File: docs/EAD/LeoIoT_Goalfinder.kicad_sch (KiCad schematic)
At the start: 38 parts, among them J1 USB_B_Micro_Breakout, J1e1 Conn_01x02_Pin, J2 LED Strip, J3 GAIN, Q1 IRFZ44N, U1 ESP32_D1_mini, U2 VL53L0X_Breakout, U3 MAX98357A_Breakout, U4 SW420_Breakout, U5 LIS3DH_Breakout

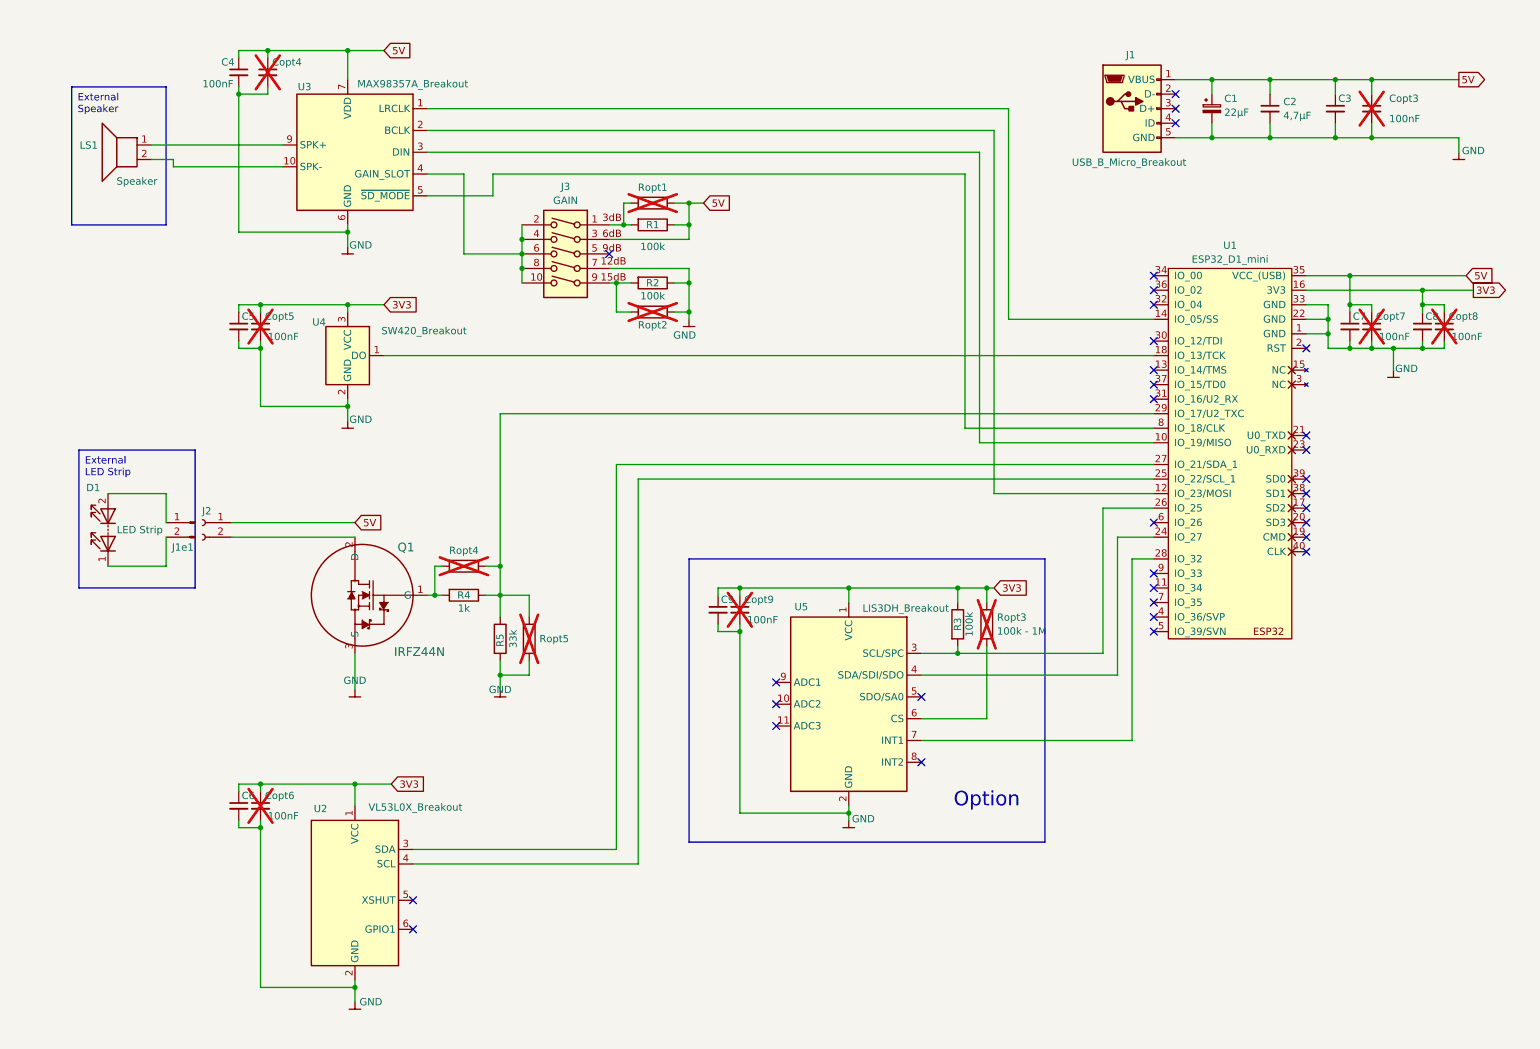
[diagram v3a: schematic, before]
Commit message: added r1.4 of PCB and SMD-only PCB layout as well as production files
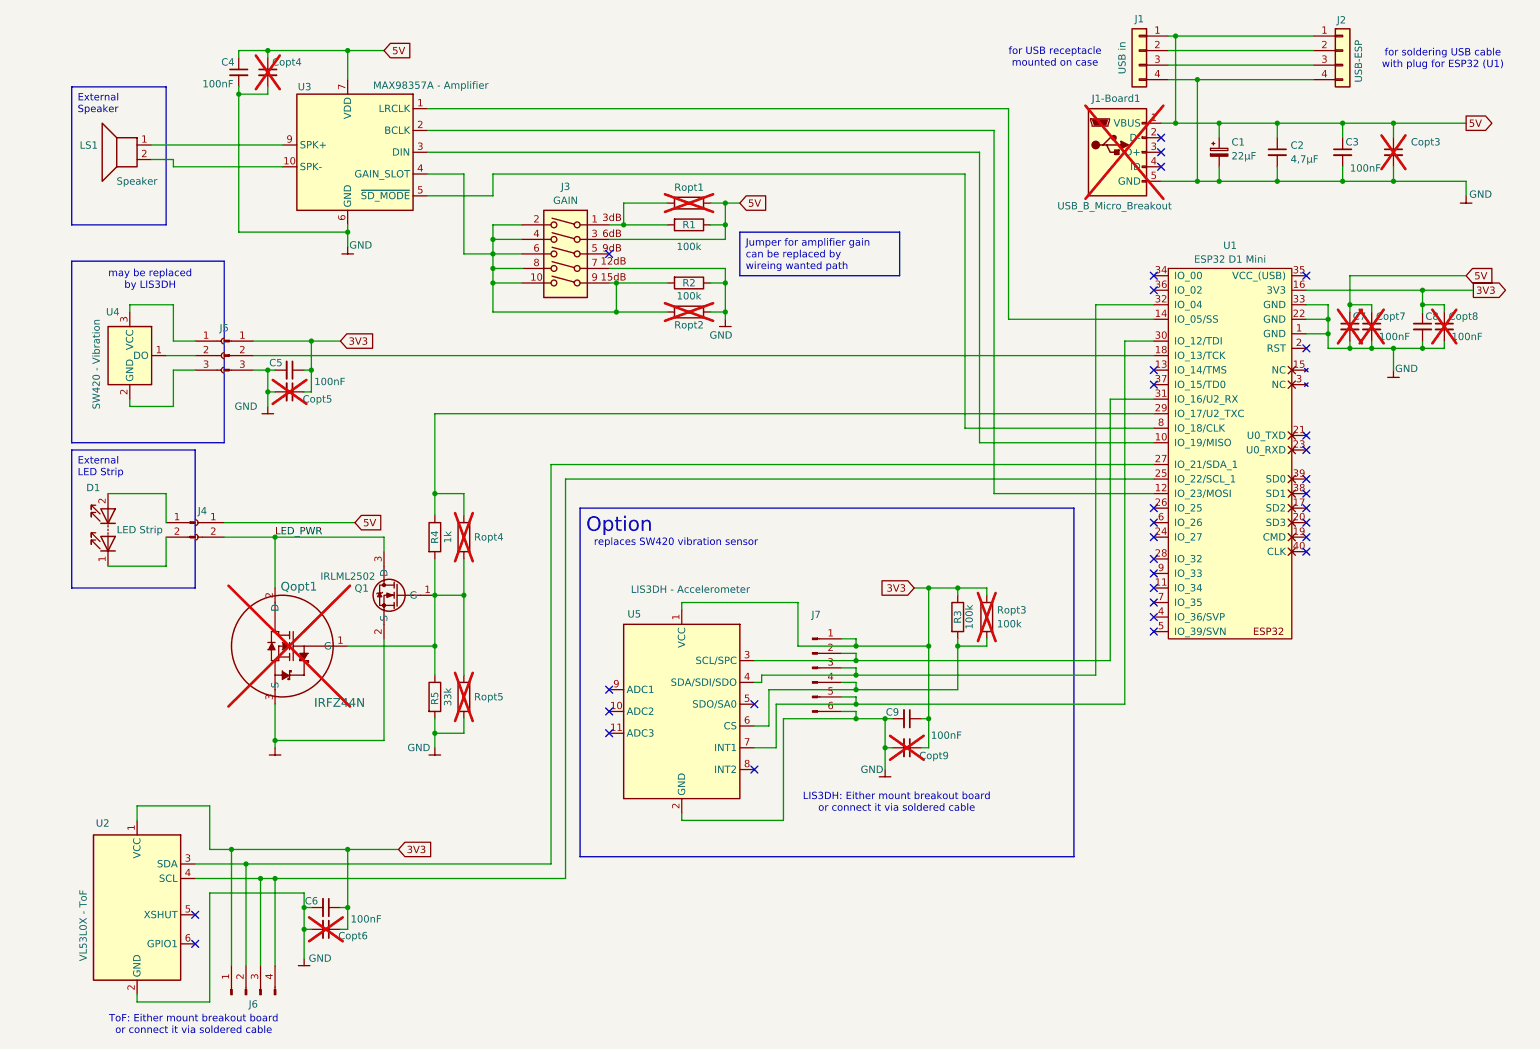
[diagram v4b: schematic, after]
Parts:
- added J1: USB in, Connector_PinHeader_2.54mm:PinHeader_1x04_P2.54mm_Vertical, symbol Connector_Generic:Conn_01x04
- added J2: USB-ESP, Connector_PinHeader_2.54mm:PinHeader_1x04_P2.54mm_Vertical, symbol Connector_Generic:Conn_01x04
- added J5: SW240 - Vcc/D0/GND, Connector_PinHeader_2.54mm:PinHeader_1x03_P2.54mm_Horizontal, symbol Connector:Conn_01x03_Pin
- added J5e1: Conn_01x03_Socket, symbol Connector:Conn_01x03_Socket
- added J6: VL53L0X-ToF Vcc/SDA/SCL/GND, Connector_PinHeader_2.54mm:PinHeader_1x04_P2.54mm_Vertical, symbol Connector:Conn_01x04_Pin
- added J7: LIS3DH, Connector_PinHeader_2.54mm:PinHeader_1x06_P2.54mm_Horizontal, symbol Connector:Conn_01x06_Pin
- added Q1: IRLML2502, Package_TO_SOT_SMD:SOT-23, symbol Transistor_FET_Own:IRLML2502
- C7: now not fitted; now left out of the parts list
- J1-Board1: renamed from J1; now not fitted
- J4: renamed from J2; footprint Connector_JST_2.54:JST_XH_B2B-XH-A_1x02_P2.54mm_Vertical -> Connector_JST:JST_XH_B2B-XH-A_1x02_P2.50mm_Vertical; now left out of the parts list
- Qopt1: renamed from Q1; now not fitted
- R3: now in the parts list
- Ropt3: value 100k - 1M -> 100k
- U1: value ESP32_D1_mini -> ESP32 D1 Mini
- U2: value VL53L0X_Breakout -> VL53L0X - ToF
- U3: value MAX98357A_Breakout -> MAX98357A - Amplifier
- U4: value SW420_Breakout -> SW420 - Vibration
- U5: value LIS3DH_Breakout -> LIS3DH - Accelerometer; now in the parts list
- renumbered J1e1 to J4e1
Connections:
- net 3V3: now also J5.1 (Pin_1), J6.1 (Pin_1), J7.1 (Pin_1); no longer U4.3 (VCC)
- net 5V: now also J1.1 (Pin_1), J2.1 (Pin_1); no longer U1.35 (VCC_(USB))
- net GND: now also J1.4 (Pin_4), J2.4 (Pin_4), J5.3 (Pin_3), J7.6 (Pin_6), Q1.2 (S); no longer U4.2 (GND)
- net at R4.1, Ropt4.1, U1.29 (IO_17/U2_TXC): no longer R5.1, Ropt5.1
- net at J3.10, J3.2, J3.4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: now also J3.9, R2.2, Ropt2.2
- net at Qopt1.1 (G), R4.2, Ropt4.2: now also R5.1, Ropt5.1, Q1.1 (G)
- net at Ropt3.2, U5.6 (CS): now also R3.2, J7.4 (Pin_4)
- net LED_PWR: now reaches J4.2 (Pin_2), Qopt1.2 (D)
- net LED_PWR: now also Q1.3 (D)
- net at U5.4 (SDA/SDI/SDO): now also U1.32 (IO_04), J7.3 (Pin_3); no longer U1.24 (IO_27)
- net at U5.7 (INT1): now also U1.30 (IO_12/TDI), J7.5 (Pin_5); no longer U1.28 (IO_32)
- net at U4.1 (DO): now also J5e1.2 (Pin_2); no longer U1.18 (IO_13/TCK)
- net at U1.27 (IO_21/SDA_1), U2.3 (SDA): now also J6.2 (Pin_2)
- net at U1.25 (IO_22/SCL_1), U2.4 (SCL): now also J6.3 (Pin_3), J6.4 (Pin_4)
- net at U1.31 (IO_16/U2_RX): now also U5.3 (SCL/SPC), J7.2 (Pin_2)
- new net: J1.2 (Pin_2), J2.2 (Pin_2)
- new net: J1.3 (Pin_3), J2.3 (Pin_3)
- new net: J5e1.3 (Pin_3), U4.2 (GND)
- new net: J5e1.1 (Pin_1), U4.3 (VCC)
- new net: J5.2 (Pin_2), U1.18 (IO_13/TCK)
- now unconnected: U1.26 (IO_25)
- no-connect marks 33 -> 34
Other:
- note added: "LIS3DH: Either mount breakout board or connect it via soldered cable"
- note added: "ToF: Either mount breakout board or connect it via soldered cable"
- note added: "for USB receptacle mounted on case"
- note added: "for soldering USB cable with plug for ESP32 (U1)"
- note added: "may be replaced by LIS3DH"
- note added: "replaces SW420 vibration sensor"
- company: HTL Leonding, SJ 23-24, 2BHIF -> HTL Leonding, Leo Cub IoT
- moved on the sheet: C1, C2, C3, C5, C6, C9, Copt3, Copt5, Copt6, Copt9, J4, R1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

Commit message: finalized Goalfinder r1.4 + added optional accelerometer + added solder pads / pins for external USB socket and USB plug to ESP32 + added 'compact' variant with only SMD components + created production files for 'compact' variant + added images, renderings and models
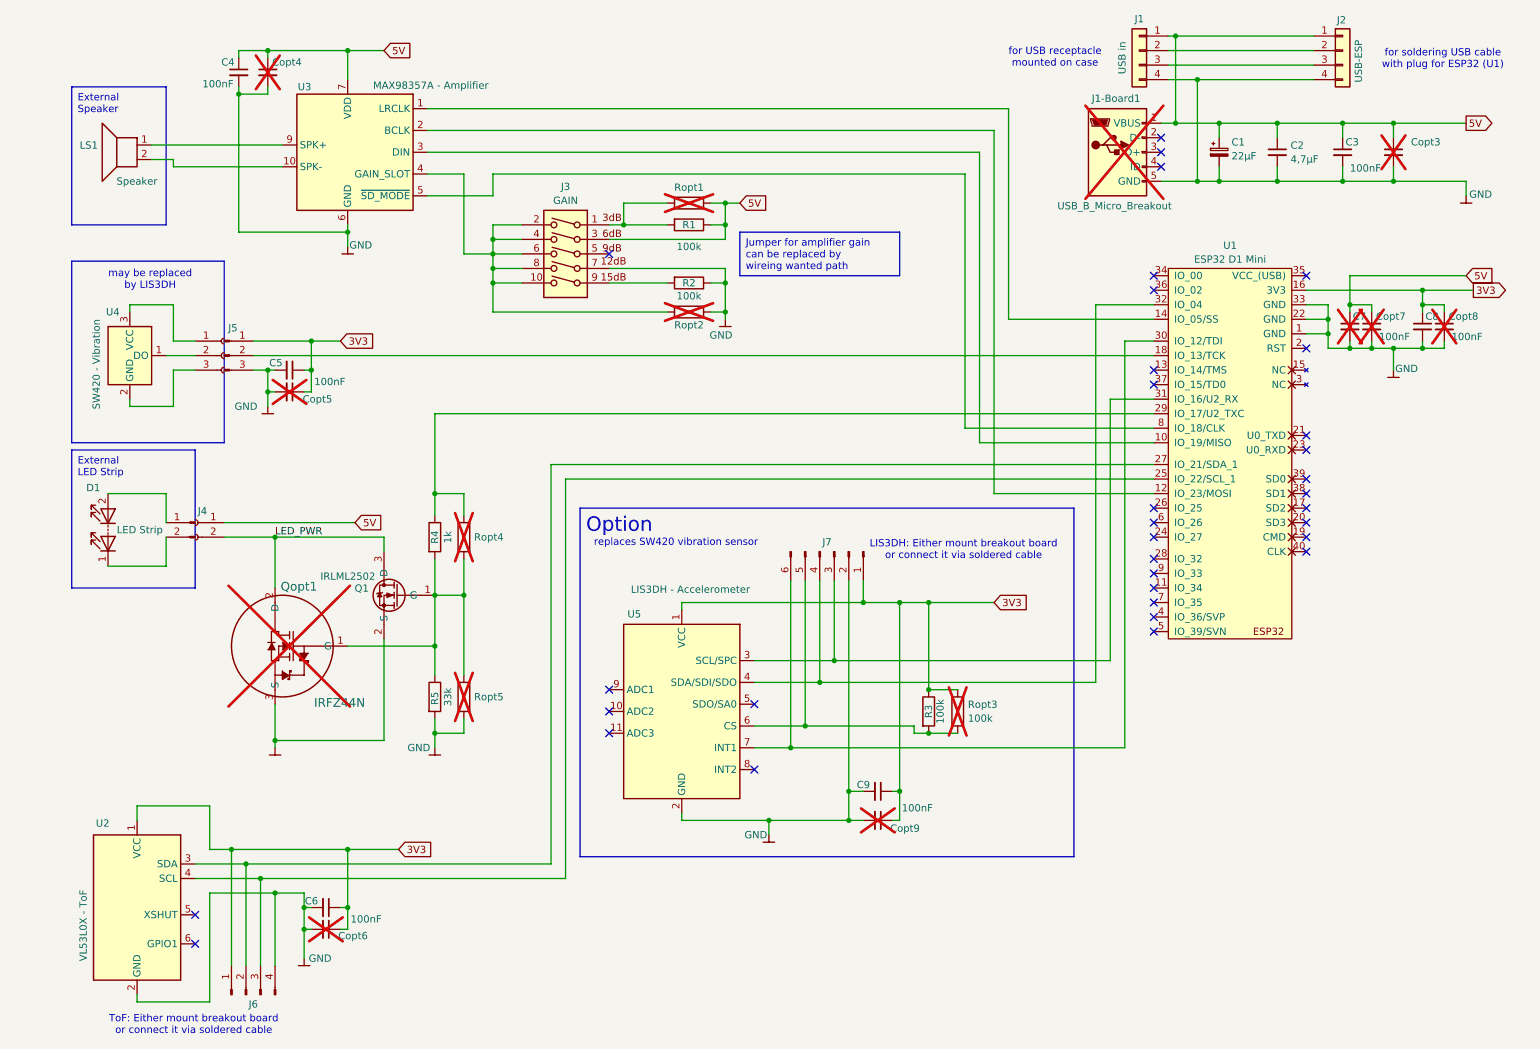
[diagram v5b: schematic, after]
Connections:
- net GND: now also J6.4 (Pin_4), J7.2 (Pin_2); no longer J7.6 (Pin_6)
- net at J3.10, J3.2, J3.4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: no longer J3.9, R2.2
- net at R3.2, Ropt3.2, U5.6 (CS): now also J7.5 (Pin_5); no longer J7.4 (Pin_4)
- net at U1.31 (IO_16/U2_RX), U5.3 (SCL/SPC): now also J7.3 (Pin_3); no longer J7.2 (Pin_2)
- net at U1.32 (IO_04), U5.4 (SDA/SDI/SDO): now also J7.4 (Pin_4); no longer J7.3 (Pin_3)
- net at U1.30 (IO_12/TDI), U5.7 (INT1): now also J7.6 (Pin_6); no longer J7.5 (Pin_5)
- net at J6.3 (Pin_3), U1.25 (IO_22/SCL_1), U2.4 (SCL): no longer J6.4 (Pin_4)
- new net: J3.9, R2.2
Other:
- moved on the sheet: C9, Copt9, J7, R3, Ropt3

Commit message: updated schematics
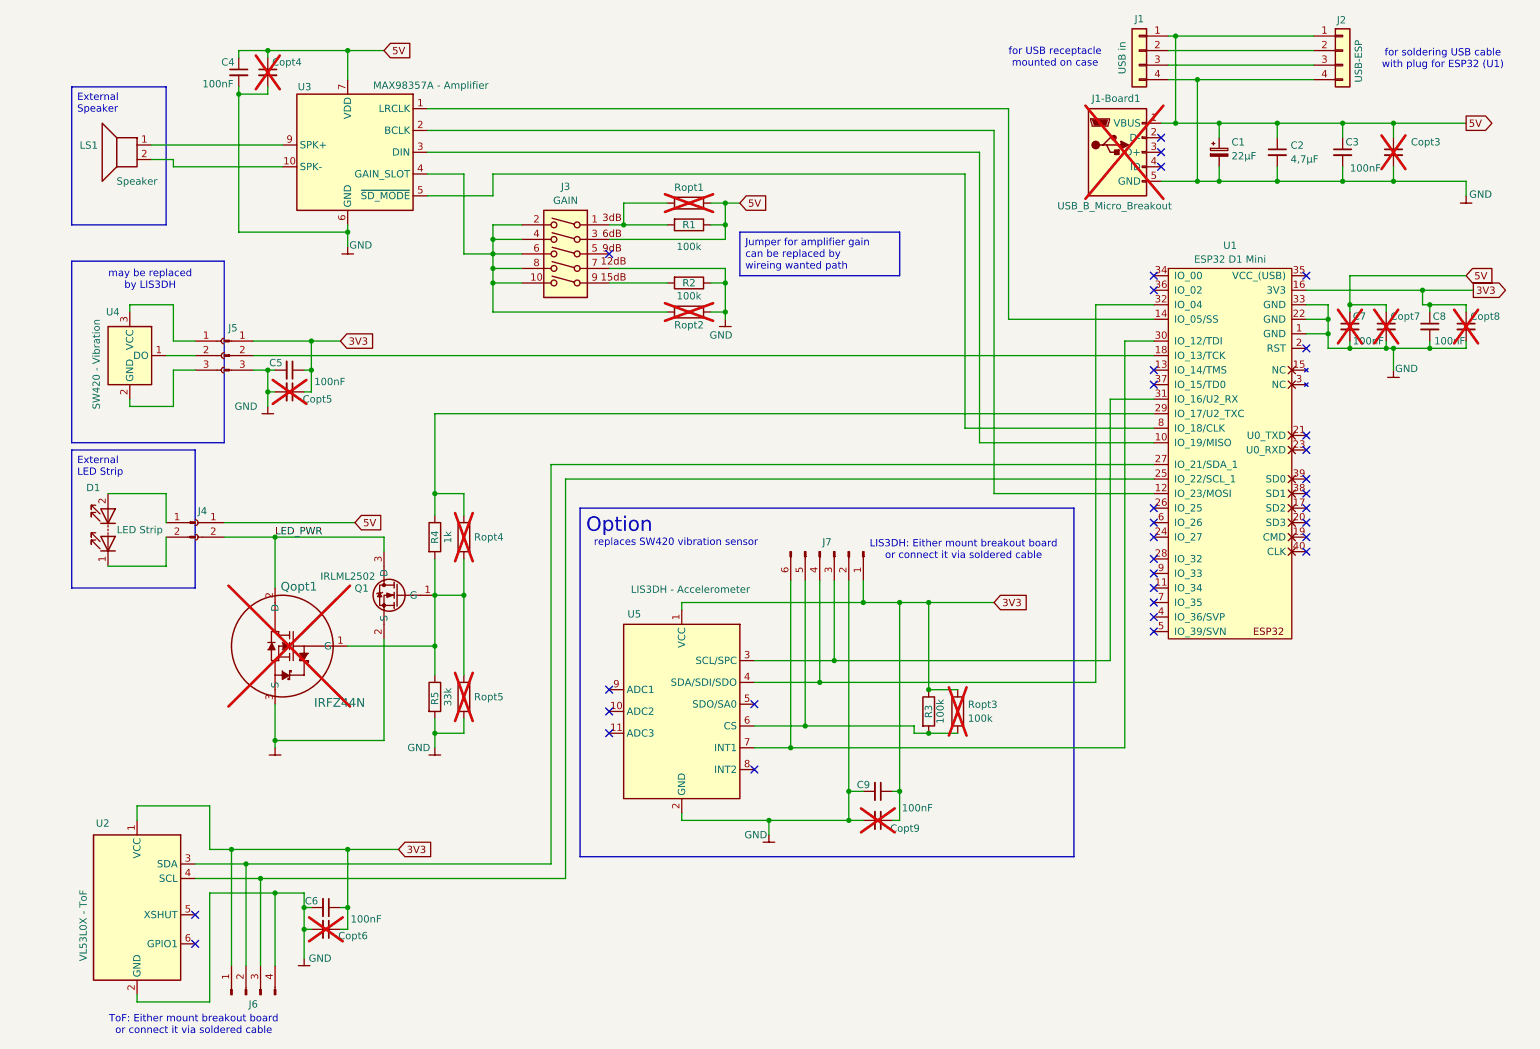
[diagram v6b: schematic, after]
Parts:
- C9: now in the parts list
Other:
- moved on the sheet: C8, Copt7, Copt8
